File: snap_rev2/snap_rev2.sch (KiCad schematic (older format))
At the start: 29 parts, among them J1 SJ2-35863B1, P1 CONN_02X05, Q1 TSM2301, SW1 1825910-6, U1 TPS610986, U2 MDBT42Q, Y1 32786Hz

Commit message: Snap rev2 updated with SMD switch, 5050 LED and bigger crystal
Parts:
- D1: value CLX6F-FKC -> 5050_RGB_LED; footprint LEDs:LED_RGB_PLCC-6 -> LEDs:LED_RGB_5050-6; symbol LED_BGR -> LED_BRG; Part Number CLX6F-FKC -> (none)
- R1: value 400 -> 400E
- R3: value 400 -> 390E
- R4: value 82 -> 82E
- R5: value 68 -> 68E
- R6: value 33 -> 33E
- R7: value 130 -> 130E
- SW1: footprint Buttons_Switches_THT:SW_TH_Tactile_Omron_B3F-10xx -> Buttons_Switches_SMD:SW_SPST_B3SL-1002P
- Y1: value 32786Hz -> ECS-3X8X; footprint Crystals:Crystal_DS10_d1.0mm_l4.3mm_Vertical -> Crystals:Crystal_C38-LF_d3.0mm_l8.0mm_Horizontal
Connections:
- net LED_GREEN: now also R6.1; no longer R5.1
- net LED_RED: now also R5.1; no longer R6.1
- net LED_SENSE: now also D1.4 (BA), R6.2; no longer D1.5 (GA), R5.2
- new net: D1.5 (GA), R5.2
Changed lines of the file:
@@
 LIBS:zetex
 LIBS:audio-jack-4_1switches
+LIBS:led_rgb
 LIBS:snap_rev2-cache
 EELAYER 26 0
@@
 P 7675 975
 F 0 "R4" V 7750 975 50  0000 C CNN
-F 1 "82" V 7675 975 50  0000 C CNN
+F 1 "82E" V 7675 975 50  0000 C CNN
 F 2 "Resistors_SMD:R_0805" V 7605 975 50  0001 C CNN
 F 3 "" H 7675 975 50  0001 C CNN
@@
 P 7675 1175
 F 0 "R5" V 7750 1175 50  0000 C CNN
-F 1 "68" V 7675 1175 50  0000 C CNN
+F 1 "68E" V 7675 1175 50  0000 C CNN
 F 2 "Resistors_SMD:R_0805" V 7605 1175 50  0001 C CNN
 F 3 "" H 7675 1175 50  0001 C CNN
@@
 P 7675 1375
 F 0 "R6" V 7750 1375 50  0000 C CNN
-F 1 "33" V 7675 1375 50  0000 C CNN
+F 1 "33E" V 7675 1375 50  0000 C CNN
 F 2 "Resistors_SMD:R_0805" V 7605 1375 50  0001 C CNN
 F 3 "" H 7675 1375 50  0001 C CNN
@@
 Text Label 8325 975  2    60   ~ 0
 LED_BLUE
+Text Label 8325 1375 2    60   ~ 0
+LED_GREEN
 Text Label 8325 1175 2    60   ~ 0
-LED_GREEN
-Text Label 8325 1375 2    60   ~ 0
 LED_RED
-Text Label 7035 1175 0    60   ~ 0
+Text Label 7025 1375 0    60   ~ 0
 LED_SENSE
 Text Label 6100 5200 1    60   ~ 0
@@
 P 8325 3900
 F 0 "R7" V 8425 3900 50  0000 C CNN
-F 1 "130" V 8325 3900 50  0000 C CNN
+F 1 "130E" V 8325 3900 50  0000 C CNN
 F 2 "Resistors_SMD:R_0805" V 8255 3900 50  0001 C CNN
 F 3 "" H 8325 3900 50  0001 C CNN
@@
 P 3525 1225
 F 0 "R1" V 3625 1225 50  0000 C CNN
-F 1 "400" V 3525 1225 50  0000 C CNN
+F 1 "400E" V 3525 1225 50  0000 C CNN
 F 2 "Resistors_SMD:R_0805" V 3455 1225 50  0001 C CNN
 F 3 "" H 3525 1225 50  0001 C CNN
@@
 $EndComp
 $Comp
-L LED_BGR D1
+L LED_BRG D1
 U 1 1 59F31729
 P 6825 1175
 F 0 "D1" H 6825 825 50  0000 C CNN
-F 1 "CLX6F-FKC" H 6825 1581 50  0000 C CNN
-F 2 "LEDs:LED_RGB_PLCC-6" H 6825 1125 50  0001 C CNN
-F 3 "http://www.cree.com/led-components/media/documents/ds-CLX6F-FKC-1352.pdf" H 6825 1125 50  0001 C CNN
-F 4 "CLX6F-FKC" H 0   0   60  0001 C CNN "Part Number"
+F 1 "5050_RGB_LED" H 6825 1581 50  0000 C CNN
+F 2 "LEDs:LED_RGB_5050-6" H 6825 1125 50  0001 C CNN
+F 3 "https://d114hh0cykhyb0.cloudfront.net/pdfs/5050-RGB.pdf" H 6825 1125 50  0001 C CNN
 	1    6825 1175
 	1    0    0    -1
@@
 F 0 "SW1" H 3200 2960 50  0000 C CNN
 F 1 "1825910-6" H 3200 2869 50  0000 C CNN
-F 2 "Buttons_Switches_THT:SW_TH_Tactile_Omron_B3F-10xx" H 3200 2725 50  0001 C CNN
-F 3 "http://www.te.com/commerce/DocumentDelivery/DDEController?Action=srchrtrv&DocNm=1825910&DocType=Customer+Drawing&DocLang=English" H 3200 2725 50  0001 C CNN
+F 2 "Buttons_Switches_SMD:SW_SPST_B3SL-1002P" H 3200 2725 50  0001 C CNN
+F 3 "https://media.digikey.com/pdf/Data%20Sheets/E-Switch%20PDFs/TL3304AF260QJ_Dwg.pdf" H 3200 2725 50  0001 C CNN
 	1    3200 2725
 	1    0    0    -1
@@
 P 5025 5600
 F 0 "Y1" H 5025 5425 50  0000 C CNN
-F 1 "32786Hz" H 5025 5750 50  0000 C CNN
-F 2 "Crystals:Crystal_DS10_d1.0mm_l4.3mm_Vertical" H 5025 5600 50  0001 C CNN
-F 3 "http://cfd.citizen.co.jp/english/prod-tech/product/pdf/datasheet_TF/CFS-206_CFS-145_E.pdf" H 5025 5600 50  0001 C CNN
+F 1 "ECS-3X8X" H 5025 5750 50  0000 C CNN
+F 2 "Crystals:Crystal_C38-LF_d3.0mm_l8.0mm_Horizontal" H 5025 5600 50  0001 C CNN
+F 3 "https://www.ecsxtal.com/store/pdf/ECS-3x8X%202x6X%201X5X.pdf" H 5025 5600 50  0001 C CNN
 	1    5025 5600
 	1    0    0    -1
@@
 P 7425 4600
 F 0 "R3" V 7525 4600 50  0000 C CNN
-F 1 "400" V 7425 4600 50  0000 C CNN
+F 1 "390E" V 7425 4600 50  0000 C CNN
 F 2 "Resistors_SMD:R_0805" V 7355 4600 50  0001 C CNN
 F 3 "" H 7425 4600 50  0001 C CNN

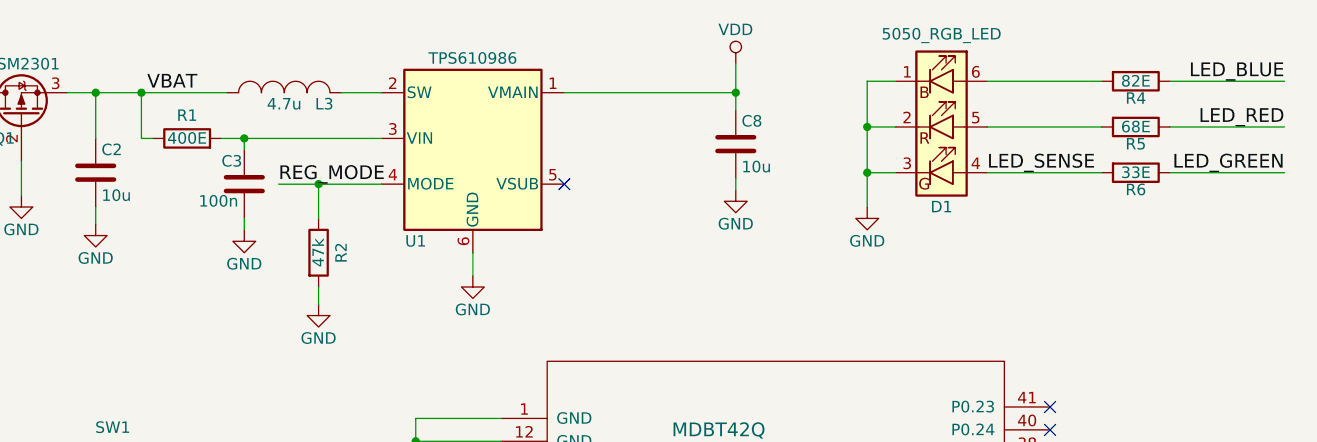
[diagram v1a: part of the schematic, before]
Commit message: TPS boost regulator's filter's R value changed to common 390E and fixes the swapped out R and G's resistor value for the RGB LED.
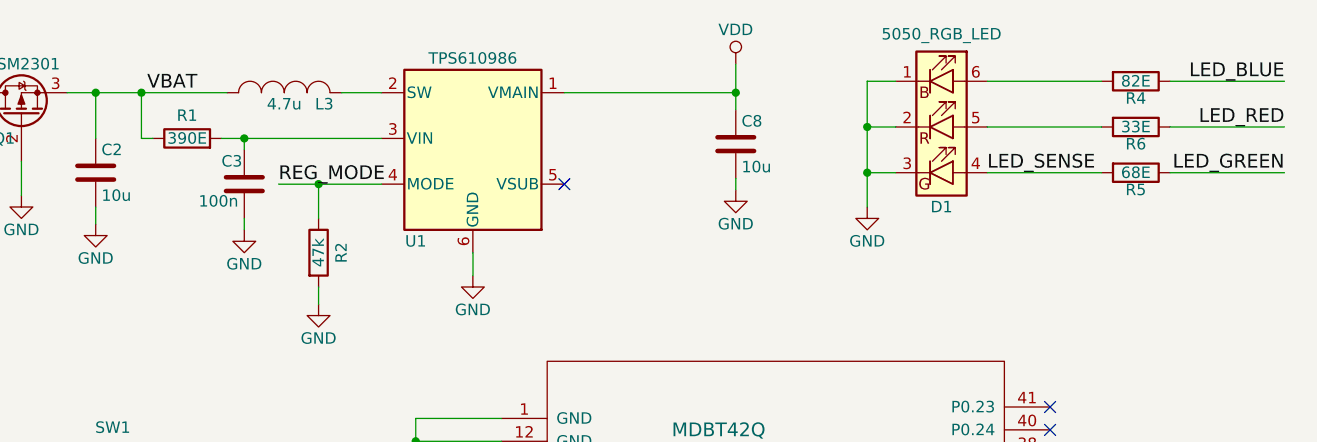
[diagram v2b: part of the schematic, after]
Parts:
- R1: value 400E -> 390E
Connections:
- net LED_GREEN: now also R5.1; no longer R6.1
- net LED_RED: now also R6.1; no longer R5.1
- net LED_SENSE: now also R5.2; no longer R6.2
- net at D1.5 (GA): now also R6.2; no longer R5.2
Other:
- moved on the sheet: R5, R6
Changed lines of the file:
@@
 L R R5
 U 1 1 59F31714
-P 7675 1175
-F 0 "R5" V 7750 1175 50  0000 C CNN
-F 1 "68E" V 7675 1175 50  0000 C CNN
-F 2 "Resistors_SMD:R_0805" V 7605 1175 50  0001 C CNN
-F 3 "" H 7675 1175 50  0001 C CNN
-	1    7675 1175
+P 7675 1375
+F 0 "R5" V 7750 1375 50  0000 C CNN
+F 1 "68E" V 7675 1375 50  0000 C CNN
+F 2 "Resistors_SMD:R_0805" V 7605 1375 50  0001 C CNN
+F 3 "" H 7675 1375 50  0001 C CNN
+	1    7675 1375
 	0    1    1    0
 $EndComp
@@
 L R R6
 U 1 1 59F31715
-P 7675 1375
-F 0 "R6" V 7750 1375 50  0000 C CNN
-F 1 "33E" V 7675 1375 50  0000 C CNN
-F 2 "Resistors_SMD:R_0805" V 7605 1375 50  0001 C CNN
-F 3 "" H 7675 1375 50  0001 C CNN
-	1    7675 1375
+P 7675 1175
+F 0 "R6" V 7750 1175 50  0000 C CNN
+F 1 "33E" V 7675 1175 50  0000 C CNN
+F 2 "Resistors_SMD:R_0805" V 7605 1175 50  0001 C CNN
+F 3 "" H 7675 1175 50  0001 C CNN
+	1    7675 1175
 	0    1    1    0
 $EndComp
@@
 P 3525 1225
 F 0 "R1" V 3625 1225 50  0000 C CNN
-F 1 "400E" V 3525 1225 50  0000 C CNN
+F 1 "390E" V 3525 1225 50  0000 C CNN
 F 2 "Resistors_SMD:R_0805" V 3455 1225 50  0001 C CNN
 F 3 "" H 3525 1225 50  0001 C CNN

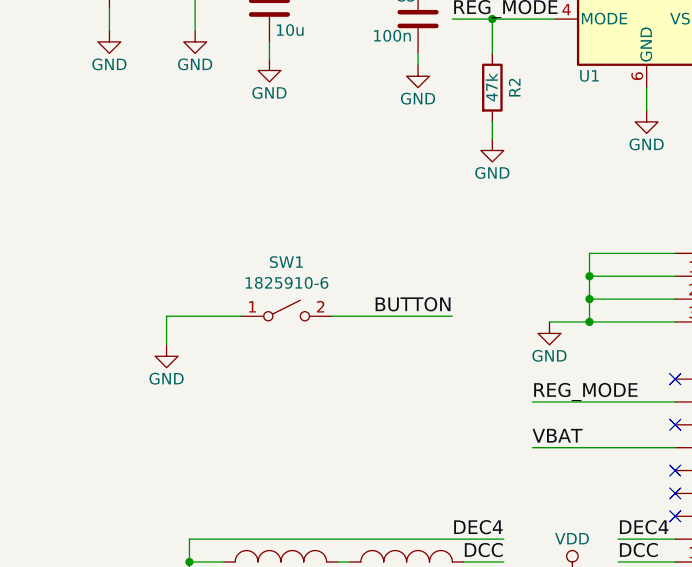
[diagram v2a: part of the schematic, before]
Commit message: Corrected the part number of the SMD tactile switch
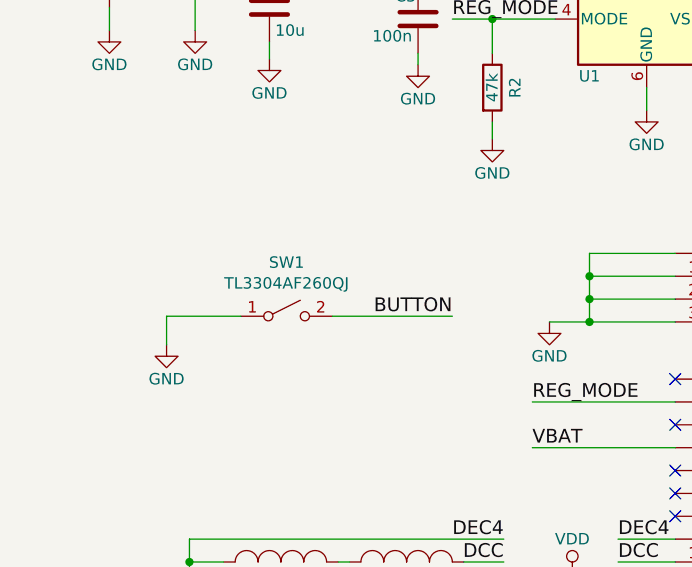
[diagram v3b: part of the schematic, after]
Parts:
- SW1: value 1825910-6 -> TL3304AF260QJ
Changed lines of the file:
@@
 P 3200 2725
 F 0 "SW1" H 3200 2960 50  0000 C CNN
-F 1 "1825910-6" H 3200 2869 50  0000 C CNN
+F 1 "TL3304AF260QJ" H 3200 2869 50  0000 C CNN
 F 2 "Buttons_Switches_SMD:SW_SPST_B3SL-1002P" H 3200 2725 50  0001 C CNN
 F 3 "https://media.digikey.com/pdf/Data%20Sheets/E-Switch%20PDFs/TL3304AF260QJ_Dwg.pdf" H 3200 2725 50  0001 C CNN
